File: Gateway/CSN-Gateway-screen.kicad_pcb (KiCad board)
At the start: 2 copper layers, 0 parts

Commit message: More work on gateway
- Add ftdi ft232rl chip for usb comms
- Remove debug connector (not used if we have usb)
- Add capa and resistors to rs485
- Draw edge cut for both bottom and top pcb at the correct size of the
case
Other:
- board outline added: 32 x 58 mm
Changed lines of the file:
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@@
     (links 0)
     (no_connects 0)
-    (area 107.442 72.610039 171.738361 134.009421)
+    (area 109.424999 63.924999 141.575001 122.075001)
     (thickness 1.6)
-    (drawings 0)
+    (drawings 4)
     (tracks 0)
     (zones 0)
@@
     (uvia_drill 0.1)
   )
+  (gr_line (start 109.5 122) (end 109.5 64) (angle 90) (layer Edge.Cuts) (width 0.15))
+  (gr_line (start 141.5 122) (end 109.5 122) (angle 90) (layer Edge.Cuts) (width 0.15))
+  (gr_line (start 141.5 64) (end 141.5 122) (angle 90) (layer Edge.Cuts) (width 0.15))
+  (gr_line (start 109.5 64) (end 141.5 64) (angle 90) (layer Edge.Cuts) (width 0.15))
 )

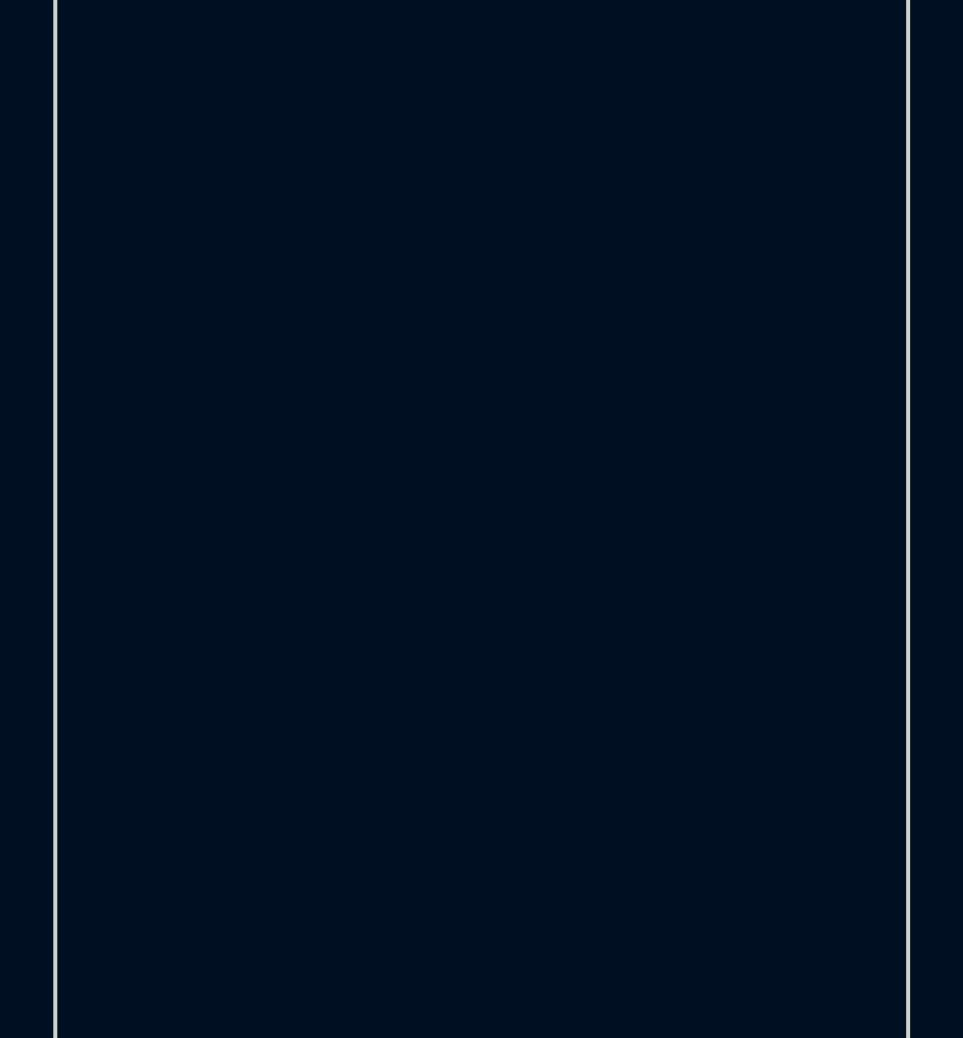
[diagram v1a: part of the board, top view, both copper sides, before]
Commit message: Split project into 2 sch + 2 pcb (screen + base)
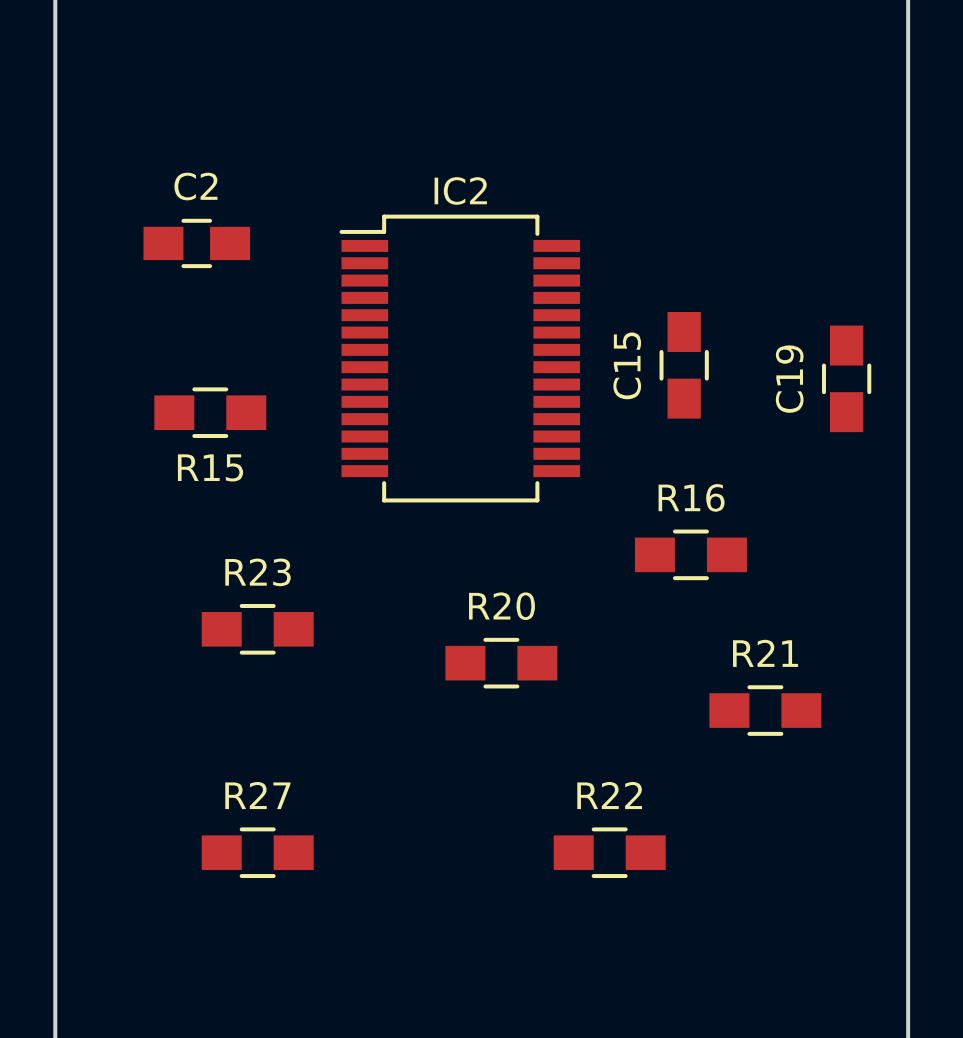
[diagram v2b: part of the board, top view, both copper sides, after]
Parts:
- added C15: 100nF, Capacitors_SMD:C_0805_HandSoldering, F.Cu at (133.1, 79.0)
- added C19: 100nF, Capacitors_SMD:C_0805_HandSoldering, F.Cu at (139.2, 79.5)
- added C2: 0.1uF, Capacitors_SMD:C_0805_HandSoldering, F.Cu at (114.8, 74.4)
- added IC2: FT232RL, Housings_SSOP:SSOP-28_5.3x10.2mm_Pitch0.65mm, F.Cu at (124.7, 78.7)
- added R15: 10K, Resistors_SMD:R_0805_HandSoldering, F.Cu at (115.3, 80.8)
- added R16: 100, Resistors_SMD:R_0805_HandSoldering, F.Cu at (133.3, 86.1)
- added R20: 4k7, Resistors_SMD:R_0805_HandSoldering, F.Cu at (126.2, 90.2)
- added R21: 10k, Resistors_SMD:R_0805_HandSoldering, F.Cu at (136.1, 91.9)
- added R22: 100, Resistors_SMD:R_0805_HandSoldering, F.Cu at (130.3, 97.3)
- added R23: 100, Resistors_SMD:R_0805_HandSoldering, F.Cu at (117.1, 88.9)
- added R27: 10K, Resistors_SMD:R_0805_HandSoldering, F.Cu at (117.1, 97.3)

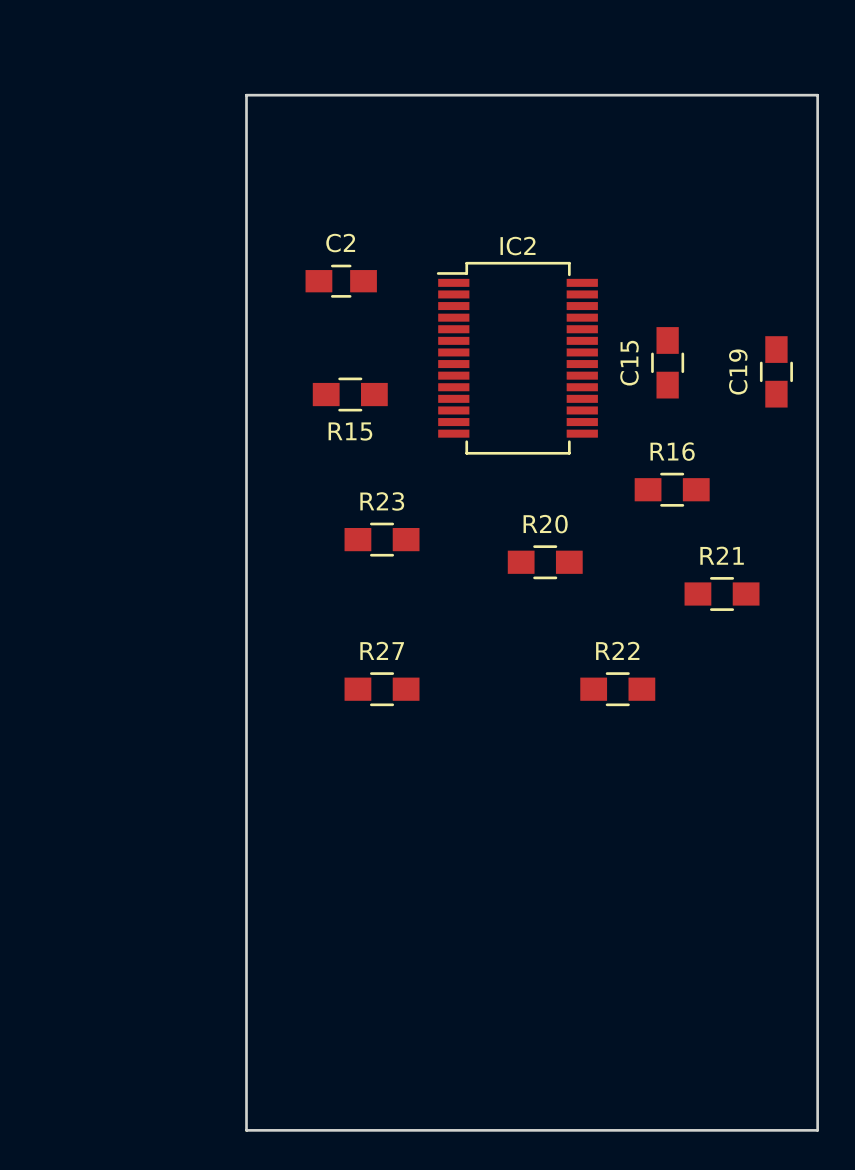
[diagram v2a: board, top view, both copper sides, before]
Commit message: add all missing footprints
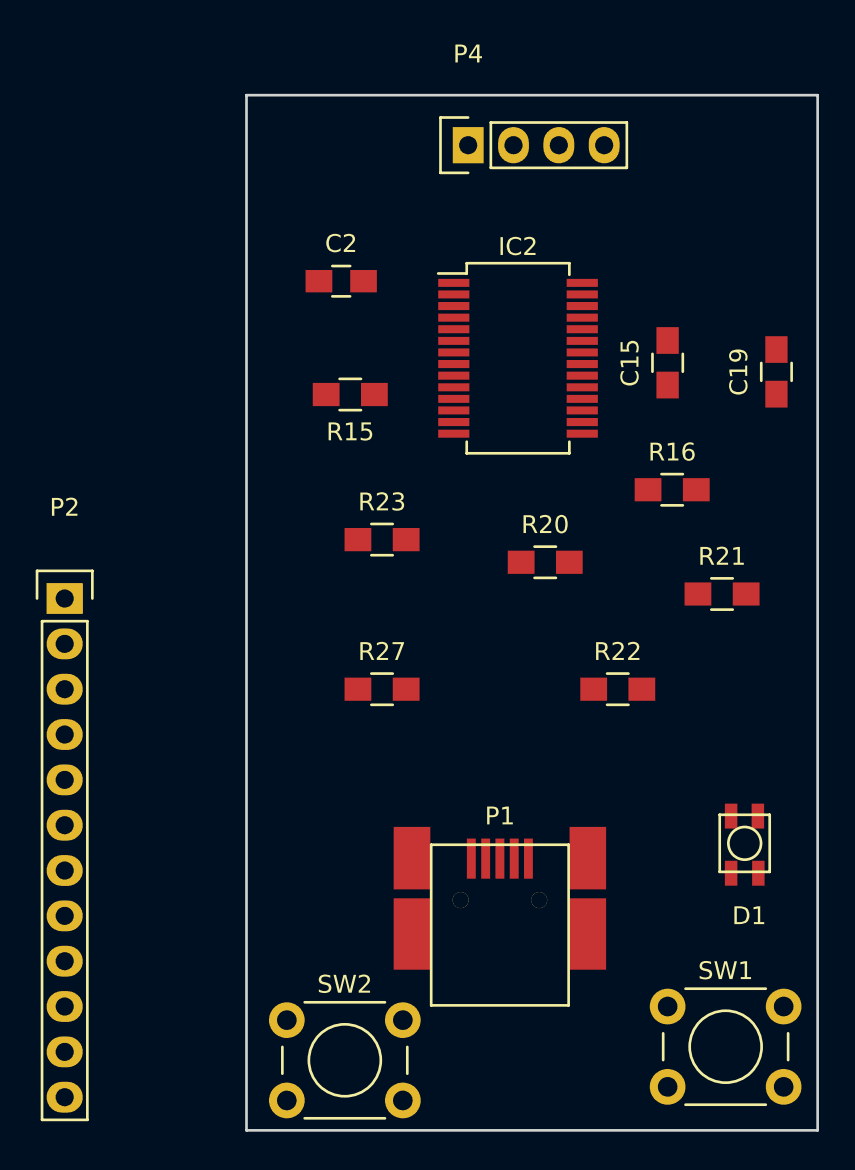
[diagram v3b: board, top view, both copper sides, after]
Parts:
- added D1: LED_RABG, footprints:LedRGB_MULTICOMP_703-1028, F.Cu at (136.7, 104.4)
- added P1: USB_MINI, footprints:MolexUSB_Mini-B_67503-1020, F.Cu at (123.7, 111.0)
- added P2: CONN_01X12, Pin_Headers:Pin_Header_Straight_1x12, F.Cu at (99.3, 92.2)
- added P4: CONN_OLED_SCREEN, Socket_Strips:Socket_Strip_Straight_1x04, F.Cu at (121.9, 66.8)
- added SW1: SW_PUSH, Buttons_Switches_ThroughHole:SW_PUSH_6mm, F.Cu at (133.1, 115.1)
- added SW2: SW_PUSH, Buttons_Switches_ThroughHole:SW_PUSH_6mm, F.Cu at (111.8, 115.8)
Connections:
- C2 pad 1: (no net) -> RST
- IC2 pad 1: (no net) -> RXI
- IC2 pad 15: (no net) -> Net-(IC2-Pad15)
- IC2 pad 16: (no net) -> Net-(IC2-Pad16)
- IC2 pad 5: (no net) -> TXO
- R15 pad 2: (no net) -> BTN1
- R16 pad 1: (no net) -> RGB1
- R16 pad 2: (no net) -> Net-(D1-Pad1)
- R20 pad 1: (no net) -> Net-(P1-Pad1)
- R22 pad 1: (no net) -> RGB2
- R22 pad 2: (no net) -> Net-(D1-Pad4)
- R23 pad 1: (no net) -> RGB3
- R23 pad 2: (no net) -> Net-(D1-Pad3)
- R27 pad 2: (no net) -> BTN2

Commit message: finish screen pcb routing
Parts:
- added REF**: MountingHole_2.2mm_M2, Mounting_Holes:MountingHole_2.2mm_M2, F.Cu at (138.4, 81.8)
- added REF**: MountingHole_2.2mm_M2, Mounting_Holes:MountingHole_2.2mm_M2, F.Cu at (113.3, 81.8)
- added REF**: MountingHole_2.2mm_M2, Mounting_Holes:MountingHole_2.2mm_M2, F.Cu at (113.3, 103.1)
- added REF**: MountingHole_3.2mm_M3, Mounting_Holes:MountingHole_3.2mm_M3, F.Cu at (137.7, 110.7)
- added REF**: MountingHole_3.2mm_M3, Mounting_Holes:MountingHole_3.2mm_M3, F.Cu at (137.7, 68.1)
- added REF**: MountingHole_3.2mm_M3, Mounting_Holes:MountingHole_3.2mm_M3, F.Cu at (113.3, 68.1)
- added REF**: MountingHole_3.2mm_M3, Mounting_Holes:MountingHole_3.2mm_M3, F.Cu at (113.3, 110.5)
- added REF**: MountingHole_2.2mm_M2, Mounting_Holes:MountingHole_2.2mm_M2, F.Cu at (138.4, 103.1)
- C15, C19, C2, IC2, P2, R20, R21: moved to B.Cu
- moved P1 43.0 mm to (125.5, 68.1), turned to 270 degrees
- moved R15 39.4 mm to (128.5, 117.9), turned to 270 degrees
- moved P2 37.1 mm to (133.6, 106.4)
- moved C2 24.9 mm to (128.5, 95.2), turned to 180 degrees
- moved C19 22.3 mm to (118.4, 87.4), turned to 180 degrees
- moved R27 21.2 mm to (122.2, 117.9), turned to 270 degrees
- moved R16 17.1 mm to (122.2, 99.1), turned to 270 degrees
- moved C15 16.0 mm to (118.4, 85.3), turned to 180 degrees
- moved R23 15.9 mm to (129.3, 99.1), turned to 270 degrees
- moved IC2 15.6 mm to (120.4, 93.7), turned to 90 degrees
- moved P4 15.0 mm to (121.7, 81.8)
- moved R21 12.8 mm to (124.2, 87.4)
- moved D1 11.7 mm to (125.0, 103.9)
- moved R20 5.24 mm to (124.2, 85.3), turned to 180 degrees
- moved R22 4.91 mm to (125.7, 99.1), turned to 270 degrees
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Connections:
- P2 pad 2: RXI -> TXO
- P2 pad 4: TXO -> RXI
- P4 pad 1: SDA -> GND
- P4 pad 2: SCL -> VCC
- P4 pad 3: GND -> SCL
- P4 pad 4: VCC -> SDA
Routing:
- net VCC: track 0.00 -> 79.5 mm, vias 0 -> 2
- net GND: track 0.00 -> 60.1 mm, vias 0 -> 2
- net BTN2: track 0.00 -> 51.5 mm
- net BTN1: track 0.00 -> 47.0 mm
- net SCL: track 0.00 -> 32.6 mm
- net Net-(IC2-Pad16): track 0.00 -> 28.7 mm, vias 0 -> 1
- net Net-(IC2-Pad15): track 0.00 -> 26.6 mm, vias 0 -> 1
- net SDA: track 0.00 -> 24.5 mm
- net RGB1: track 0.00 -> 23.8 mm
- net RGB2: track 0.00 -> 20.3 mm
- net Net-(P1-Pad1): track 0.00 -> 19.4 mm, vias 0 -> 1
- net TXO: track 0.00 -> 19.0 mm
- net RGB3: track 0.00 -> 14.0 mm, vias 0 -> 1
- net Net-(IC2-Pad19): track 0.00 -> 12.2 mm, vias 0 -> 2
- net RXI: track 0.00 -> 9.60 mm
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- added copper zone on B.Cu, net GND
- added copper zone on F.Cu, net GND

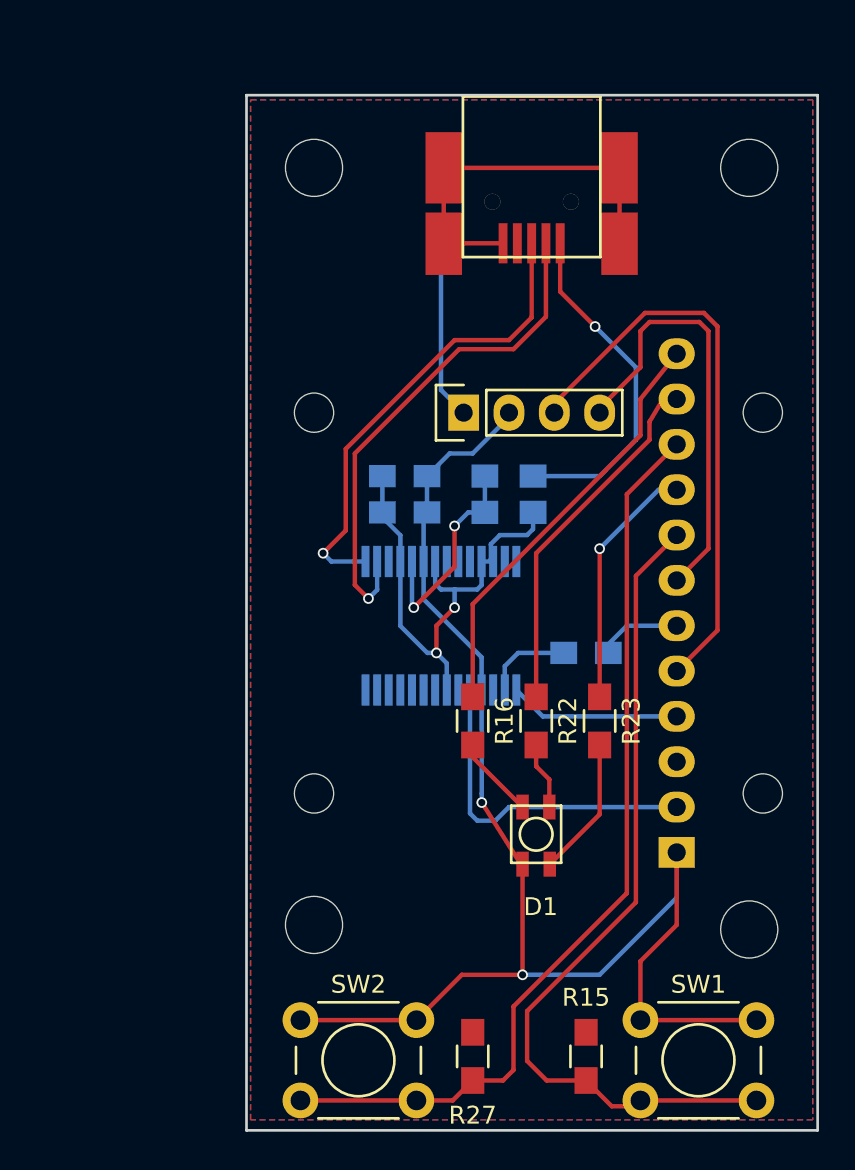
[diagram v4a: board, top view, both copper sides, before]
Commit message: Finish base pcb routing and adjust all mounting holes
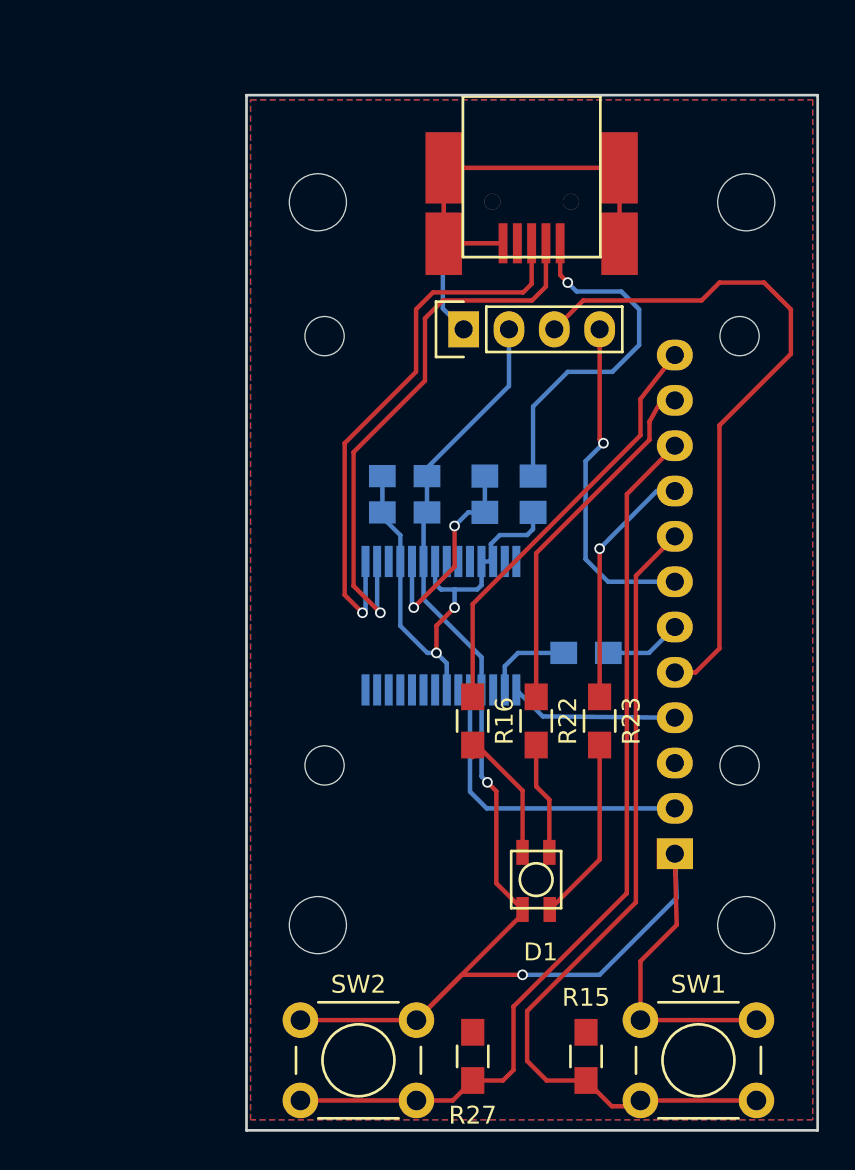
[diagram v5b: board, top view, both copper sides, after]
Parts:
- moved P4 4.67 mm to (121.7, 77.1)
- moved REF** 4.48 mm to (137.1, 77.5)
- moved REF** 4.33 mm to (113.9, 77.5)
- moved D1 2.54 mm to (125.0, 106.4)
- moved REF** 2.04 mm to (137.1, 101.6)
- moved REF** 1.94 mm to (113.5, 70.0)
- moved REF** 1.94 mm to (137.5, 70.0)
- moved REF** 1.68 mm to (113.9, 101.6)
- moved REF** 0.30 mm to (137.5, 110.5)
- moved REF** 0.22 mm to (113.5, 110.5)
- moved P2 0.13 mm to (133.5, 106.5)
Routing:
- net VCC: track 79.5 -> 88.5 mm
- net SCL: track 32.6 -> 38.9 mm
- net SDA: track 24.5 -> 18.9 mm, vias 0 -> 2
- net GND: track 60.1 -> 55.3 mm
- net Net-(IC2-Pad15): track 26.6 -> 31.4 mm
- net Net-(D1-Pad1): track 4.63 -> 7.99 mm
- net Net-(IC2-Pad16): track 28.7 -> 31.7 mm
- net Net-(D1-Pad4): track 3.78 -> 6.32 mm
- net Net-(D1-Pad3): track 7.83 -> 10.4 mm
- net TXO: track 19.0 -> 17.6 mm
- net Net-(P1-Pad1): track 19.4 -> 20.3 mm

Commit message: add silkscreen infos on pcb
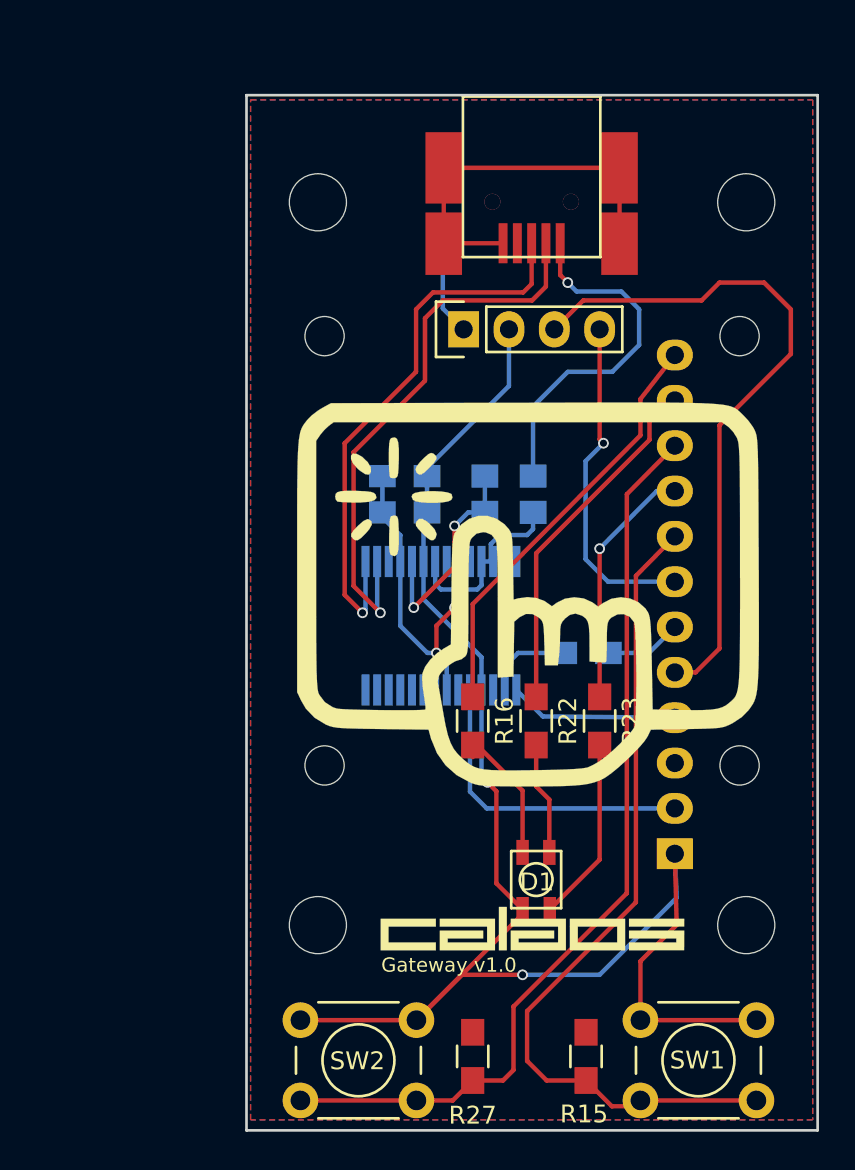
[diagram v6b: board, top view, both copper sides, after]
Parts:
- added G***: LOGO, libs:calaos_logo_small, F.Cu at (125.2, 92.0)
- added G***: LOGO, libs:calaos_logo_single, F.Cu at (125.5, 110.7)
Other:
- board text added: "BTN1"
- board text added: "BTN2"
- board text added: "GND"
- board text added: "Gateway v1.0"
- board text added: "RGB1"
- board text added: "RGB2"
- board text added: "RGB3"
- board text added: "RST"
- board text added: "RXI"
- board text added: "SCL"
- board text added: "SDA"
- board text added: "TXO"
- board text added: "VCC"
